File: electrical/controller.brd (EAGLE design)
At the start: 101.6 x 25.4 mm, 39 parts, among them IC1 555, IC2 MCP4728, J3 455-1750-1-ND, Q1 DMP3098, Q2 DMG3402L-7, Q3 600mA/40V, Q4 DMP3098, U1 U3V16F15, U2 U3V16F15, U5 MCP6042, U6 MCP6042

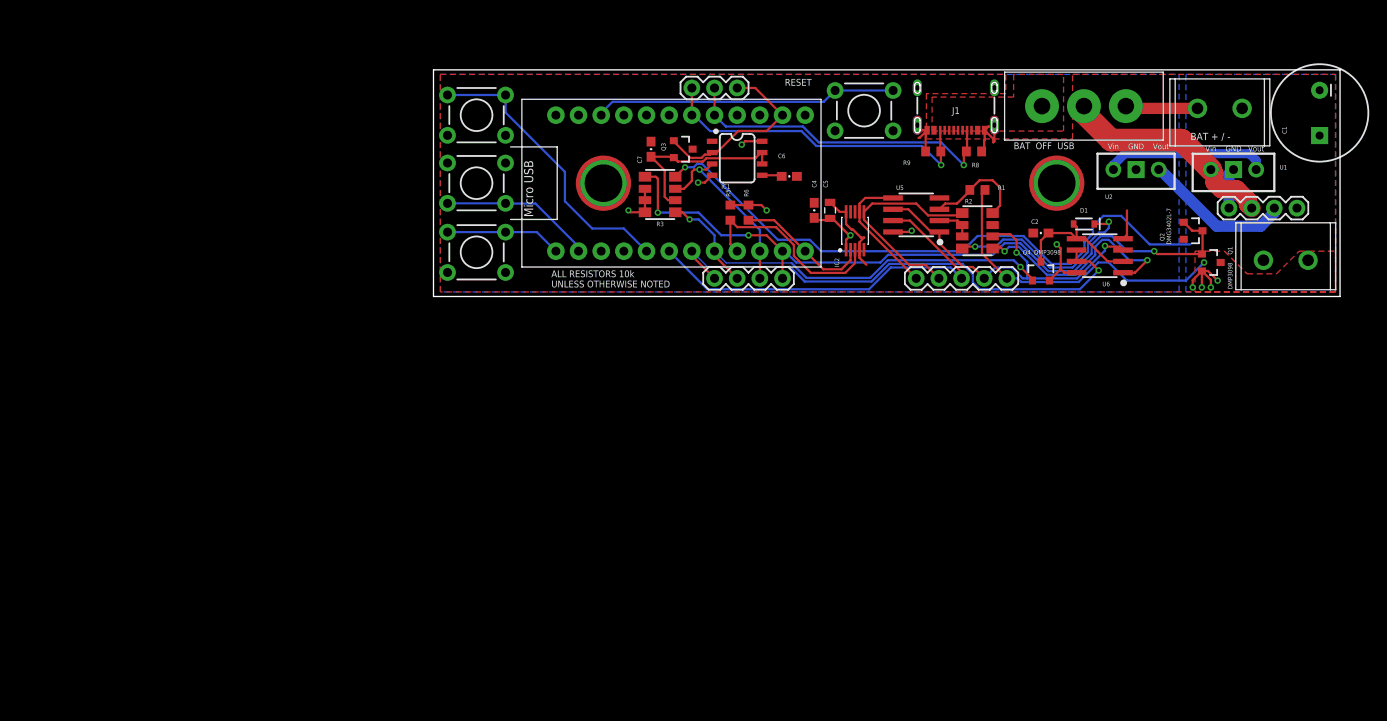
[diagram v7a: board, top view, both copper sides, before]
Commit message: Massive SCH changes for Rev D3
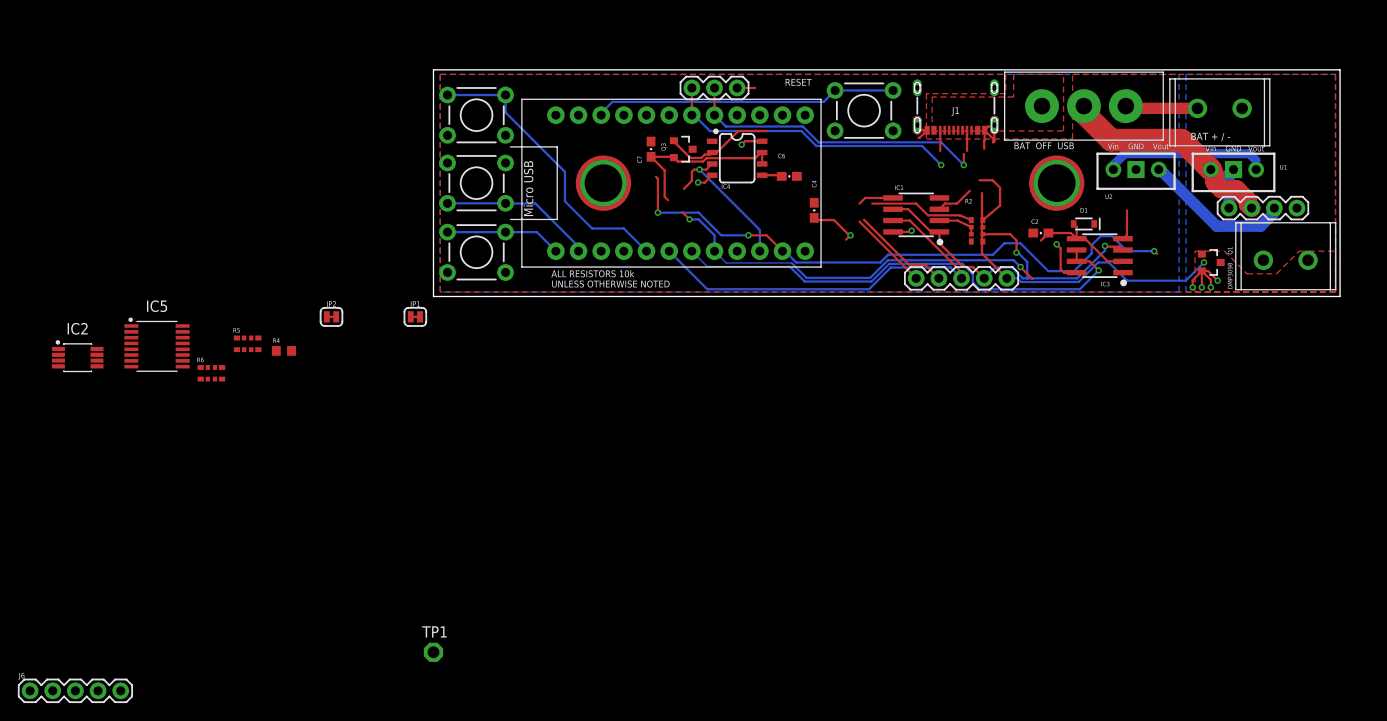
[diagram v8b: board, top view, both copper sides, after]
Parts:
- removed C1: 1000uF, SparkFun-Capacitors:CPOL-RADIAL-1000UF-25V
- removed C5: 10uF, pie:0805
- removed J5: (no value), SparkFun-Connectors:1X04
- removed Q2: DMG3402L-7, BEST_Custom:SOT23-3
- removed Q4: DMP3098, BEST_Custom:SOT23-3
- removed R1: 110k, pie:R0603
- removed R3: 1M, BEST_Custom:2012-ARV
- removed R8, R9: 5.1K, pie:R0603
- removed U5: MCP6042, BEST_Custom:SO08
- added IC4: ICM7555, SparkFun-IC-Special-Function:SO08
- added IC5: CD40109B, BEST_Custom:SOP65P640X120-16N
- added J6: (no value), SparkFun-Connectors:1X05
- added JP1, JP2: JUMPER-SMT_2_NC_TRACE_SILK, SparkFun-Jumpers:SMT-JUMPER_2_NC_TRACE_SILK
- added R4: 220, BEST_Custom:R0603
- added TP1: TPSPAD1-13, testpad:P1-13
- C2, C4: value .1uF -> 0.033uF
- C6: value 0.01 uF -> 0.033uF
- D1: value 250mA/100V -> 250mA/100V/350mV
- IC1: value 555 -> MCP6232; device SparkFun-IC-Special-Function:SO08 -> BEST_Custom:SO08
- IC2: value MCP4728 -> LTC1661MSOP8; device BEST_Custom:SOP50P495X110-10N -> BEST_Custom:SOP65P490X110-8N
- IC3: value MCP6042 -> MCP6232
- R2: value 22k -> 50k; device BEST_Custom:2012-ARV -> BEST_Custom:1206_RA
- R5: value 10K -> 5.1k; device pie:R0603 -> BEST_Custom:1206_RA
- R6: value 10K -> 220k; device pie:R0603 -> BEST_Custom:1206_RA
- moved IC2 88.3 mm to (-39.9, -6.86), turned to 0 degrees
- moved R6 62.8 mm to (-24.9, -8.64), turned to 0 degrees
- moved R5 56.1 mm to (-20.8, -5.33), turned to 0 degrees
- moved IC1 21.0 mm to (54.1, 9.14), turned to 90 degrees
- renumbered U6 to IC3
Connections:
- removed net SCL: IC2.2, R6.1, UC1.9
- removed net SDA: IC2.3, R5.1, UC1.6
- new net 12V: IC5.16, JP1.1
- new net CS: IC2.1, UC1.10
- new net DEBUG_WAKE: J6.5, UC1.9
- new net MISO: UC1.14
- new net MOSI: IC2.3, UC1.16
- new net N$10: R6.P4, R6.P6
- new net N$11: IC5.4, Q1.1
- new net N$8: JP1.2, U1.VOUT
- new net N$9: JP2.2, U2.VOUT
- new net SCK: IC2.2, UC1.15
- net 15V: no longer C1.+, R3.4, U1.VOUT
- net 5V: now also IC2.4, IC2.6, IC4.4, IC4.8, IC5.1, IC5.2, JP2.1, R6.P5; no longer C5.1, IC1.4, IC2.1, Q4.2, R3.6, R3.7, R3.8, R5.2, R6.2, U2.VOUT, U5.8
- net A_PEAK: now also J6.4; no longer J5.4
- net CC1: now also R5.P1; no longer R8.1
- net CC2: now also R5.P2; no longer R9.1
- net COIL: now also R6.P1; no longer R1.1
- net DRIVE: now also IC5.3, J6.1; no longer J5.1, Q1.1, Q2.1, Q2.3, R3.5
- net GND: now also IC1.4, IC2.7, IC4.1, IC5.10, IC5.14, IC5.15, IC5.6, IC5.7, IC5.8, IC5.9, R2.P3, R5.P7, R5.P8; no longer C1.-, C5.2, IC1.1, IC2.10, IC2.4, Q2.2, R2.3, R8.2, R9.2, U5.4
- net INT: now also IC1.7; no longer U5.7
- net N$1: now also D1.C, R4.2; no longer C2.1, D1.A, IC3.2, IC3.5, Q4.3
- net N$2: now also R4.1; no longer R2.1
- net N$3: now also R6.P3, R6.P7; no longer D1.C, R2.8
- net N$4: now also IC1.3, R2.P4, R6.P8; no longer R1.2, R2.4, U5.3
- net N$5: now also IC1.2, R2.P6, R2.P7; no longer R2.6, R2.7, U5.2
- net N$6: now also IC4.5; no longer IC1.5
- net N$7: now also IC4.6, IC4.7, R6.P2, TP1.TP; no longer IC1.6, IC1.7, R3.2
- net PEAK_RST: now also C2.1, D1.A, IC3.2, IC3.5, J6.3; no longer J5.3, Q4.1, R3.1
- net SHIFT: now also IC1.1, IC1.6, R2.P2; no longer R2.2, U5.1, U5.6
- net TIMER_RESTART: now also IC4.3, J6.2; no longer IC1.3, J5.2, R3.3
- net TIMER_RST: now also IC4.2, UC1.6; no longer IC1.2, UC1.16
- net V1: now also IC2.8, R2.P5; no longer IC2.6, R2.5
- net V2: now also IC1.5, IC2.5; no longer IC2.7, U5.5
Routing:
- net 15V: track 96.1 -> 26.1 mm, vias 5 -> 4
- net N$2: track 25.6 -> 0.00 mm, vias 2 -> 0
- net N$3: track 23.0 -> 0.00 mm, vias 2 -> 0
- net SDA: track 22.9 -> 0.00 mm
- net SCL: track 15.3 -> 0.00 mm
- net N$1: track 15.0 -> 0.00 mm
- net DRIVE: track 82.0 -> 67.6 mm
- net GND: track 30.3 -> 17.9 mm
- net 5V: track 45.6 -> 33.6 mm, vias 7 -> 5
- net PEAK_RST: track 50.1 -> 58.2 mm
- net TIMER_RST: track 21.4 -> 14.5 mm
- net TIMER_RESTART: track 20.9 -> 16.9 mm
- net A_PEAK: track 58.7 -> 55.1 mm
- net V2: track 15.0 -> 13.0 mm
- net CC2: track 37.2 -> 35.7 mm
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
